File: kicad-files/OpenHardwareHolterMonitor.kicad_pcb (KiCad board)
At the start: 8 copper layers, 165 x 130 mm, 127 parts, among them CON1 Micro_SD_Card, J1 Conn_01x14, J10 Conn_01x01, J11 Conn_01x01, J12 USB_OTG, J13 USB_C_Receptacle, J2 Conn_01x01, J3 Conn_01x01, J4 Conn_01x01, J5 Conn_01x01, J6 Conn_01x01, J7 Conn_01x01, J8 Conn_01x01, J9 Conn_01x01, P1 Custom_FTDI, Q1 S8050, Q2 S8050, Q3 Q_NMOS_DGS, Q4 Q_NMOS_DGS, SW1 SW_SPDT, U1 ESP-WROOM-32, U2 ADS1298, U3 MCP73833, U4 MCP73833, U5 TPS2113A, U6 LP5912, U7 REM_3-xxxxS, Y1 32768Hz

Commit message: un-isolated power layout
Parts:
- added D11: LED, LEDs:LED_0603_HandSoldering, F.Cu at (206.4, 23.0)
- added D12: D_Schottky, Diodes_SMD:D_SOD-323_HandSoldering, F.Cu at (315.7, -50.1)
- added D13: D_Schottky, Diodes_SMD:D_SOD-323_HandSoldering, F.Cu at (325.9, -57.2)
- added D14: D_Schottky, Diodes_SMD:D_SOD-323_HandSoldering, F.Cu at (305.4, -43.1)
- added Q10: Q_PMOS_DGS, TO_SOT_Packages_SMD:SOT-23_Handsoldering, F.Cu at (306.4, -49.5)
- added Q5: Q_NMOS_DGS, TO_SOT_Packages_SMD:SOT-23W_Handsoldering, F.Cu at (296.1, -56.5)
- added Q6: Q_NMOS_DGS, TO_SOT_Packages_SMD:SOT-23W_Handsoldering, F.Cu at (296.1, -49.5)
- added Q7: Q_PMOS_DGS, TO_SOT_Packages_SMD:SOT-23_Handsoldering, F.Cu at (316.6, -56.5)
- added Q8: Q_PMOS_DGS, TO_SOT_Packages_SMD:SOT-23_Handsoldering, F.Cu at (306.4, -56.5)
- added Q9: Q_PMOS_DGS, TO_SOT_Packages_SMD:SOT-23_Handsoldering, F.Cu at (296.1, -42.4)
- added R37: 100k, Resistors_SMD:R_0603_HandSoldering, F.Cu at (322.3, -50.5)
- added R38: 100k, Resistors_SMD:R_0603_HandSoldering, F.Cu at (312.0, -43.5)
- added R39: 330, Resistors_SMD:R_0603_HandSoldering, F.Cu at (326.7, -41.7)
- added R40: 330, Resistors_SMD:R_0603_HandSoldering, F.Cu at (322.3, -45.5)
- added R41: 100k, Resistors_SMD:R_0603_HandSoldering, F.Cu at (326.7, -51.8)
- added R42: 100k, Resistors_SMD:R_0603_HandSoldering, F.Cu at (316.4, -44.7)
- added R43: 100k, Resistors_SMD:R_0603_HandSoldering, F.Cu at (320.8, -40.4)
- D7: value D_Schottky -> LED; footprint Diodes_SMD:D_SOD-323_HandSoldering -> LEDs:LED_0603_HandSoldering
- moved C40 159.0 mm to (202.2, -12.4)
- moved D3 159.0 mm to (222.2, -37.9)
- moved Q1 159.0 mm to (166.8, -42.8)
- moved Q4 159.0 mm to (198.2, -24.9)
- moved R12 159.0 mm to (178.8, -31.1)
- moved R27 159.0 mm to (213.4, -36.9)
- moved R28 159.0 mm to (203.8, -40.8)
- moved R29 159.0 mm to (195.6, -35.0)
- moved R30 159.0 mm to (208.8, -20.5)
- moved R31 159.0 mm to (165.8, -31.9)
- moved R32 159.0 mm to (215.6, -20.9)
- moved R34 159.0 mm to (202.1, -10.9)
- moved R7 159.0 mm to (188.2, -31.7)
- moved SW1 159.0 mm to (174.8, -37.9)
- moved TH1 159.0 mm to (192.4, -1.50)
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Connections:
- BT1 pad 1: /Vbat2 -> Net-(BT1-Pad1)
- BT2 pad 1: /Vbat1 -> Net-(BT2-Pad1)
- D6 pad 2: /Vbat2 -> Net-(D6-Pad2)
- D7 pad 1: /power/REGULATOR_IN -> /power/Bat1_backwards
- D7 pad 2: /Vbat1 -> GND
- J1 pad 10: /IO27 -> /IO36
- J1 pad 11: /IO36 -> /IO39
- J1 pad 12: /IO39 -> /Enable_Charging
- J1 pad 9: /IO26 -> /IO27
- R29 pad 2: GND -> Net-(Q6-Pad1)
- R30 pad 2: GND -> Net-(Q5-Pad1)
- R36 pad 1: GND -> Net-(D9-Pad1)
- R36 pad 2: Net-(D9-Pad1) -> GND
- U1 pad 11: /IO26 -> /Enable_Charging
- U3 pad 10: /Vbat2 -> Net-(D6-Pad2)
- U3 pad 9: /Vbat2 -> Net-(D6-Pad2)
- U4 pad 10: /Vbat1 -> Net-(D12-Pad2)
- U4 pad 9: /Vbat1 -> Net-(D12-Pad2)

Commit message: board layout checkpoint
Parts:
- added TP5: Test_Point, Measurement_Points:Measurement_Point_Square-SMD-Pad_Small, F.Cu at (244.5, -66.0)
- added TP6: Test_Point, Measurement_Points:Measurement_Point_Square-SMD-Pad_Small, F.Cu at (236.3, -60.0)
- added TP7: Test_Point, Measurement_Points:Measurement_Point_Square-SMD-Pad_Small, F.Cu at (236.3, -66.0)
- J1: value Conn_01x14 -> Conn_02x06_Odd_Even; footprint Pin_Headers:Pin_Header_Straight_1x14_Pitch2.54mm -> Pin_Headers:Pin_Header_Straight_2x06_Pitch1.27mm
- TP1, TP2, TP3, TP4: value TEST -> Test_Point; footprint Measurement_Points:Measurement_Point_Round-SMD-Pad_Small -> Measurement_Points:Measurement_Point_Square-SMD-Pad_Small
- moved P1 33.5 mm to (171.5, 23.0), turned to 180 degrees
- moved CON1 33.0 mm to (182.5, 27.5)
- moved C38 28.3 mm to (172.0, 85.0)
- moved J1 23.3 mm to (150.0, 42.5)
- moved C34 22.0 mm to (146.0, 72.2)
- moved C35 22.0 mm to (146.0, 63.0)
- moved C37 22.0 mm to (146.0, 82.0)
- moved U1 15.0 mm to (156.0, 30.5), turned to 90 degrees
- moved U5 14.1 mm to (158.5, 83.5)
- moved FL1 13.5 mm to (167.0, 76.5)
- moved R35 13.5 mm to (155.0, 76.5)
- moved U7 13.4 mm to (164.0, 58.0)
- moved D8 13.0 mm to (166.0, 64.4)
- moved C39 12.7 mm to (159.5, 66.0)
- moved C41 12.7 mm to (159.0, 61.0)
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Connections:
- J1 pad 10: /IO36 -> /IO27
- J1 pad 11: /IO39 -> /IO36
- J1 pad 12: /Enable_Charging -> /IO39
- J1 pad 2: +3V3 -> GND
- J1 pad 3: /IO2 -> +3V3
- J1 pad 4: /IO4 -> /IO2
- J1 pad 5: /IO12 -> /IO4
- J1 pad 6: /IO13 -> /IO12
- J1 pad 7: /IO14 -> /IO13
- J1 pad 8: /IO15 -> /IO14
- J1 pad 9: /IO27 -> /IO15
- TP1 pad 1: Net-(TP1-Pad1) -> /Enable_Charging
- TP2 pad 1: Net-(TP2-Pad1) -> /Vbat1
- TP3 pad 1: Net-(TP3-Pad1) -> /Vbat2
- U3 pad 4: Net-(TP1-Pad1) -> Net-(TP5-Pad1)
- U3 pad 7: Net-(TP3-Pad1) -> Net-(TP7-Pad1)
- U4 pad 4: Net-(TP2-Pad1) -> Net-(TP4-Pad1)
- U4 pad 7: Net-(TP4-Pad1) -> Net-(TP6-Pad1)

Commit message: checkpoint PCB
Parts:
- moved R35 3.16 mm to (156.0, 73.5), turned to 0 degrees
- moved U5 2.92 mm to (157.0, 81.0), turned to 270 degrees
- moved P1 1.12 mm to (171.0, 22.0)
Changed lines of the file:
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@@
   (general
     (thickness 1.6)
-    (drawings 17)
+    (drawings 16)
     (tracks 336)
     (zones 0)
@@
   )
   (module Pin_Headers:Pin_Header_Straight_1x07_Pitch2.54mm (layer B.Cu)
-    (at 171.5 23 180)
+    (at 171 22 180)
     (descr "Through hole straight pin header, 1x07, 2.54mm pitch, single row")
     (tags "Through hole pin header THT 1x07 2.54mm single row")
@@
   )
   (module Resistors_SMD:R_0603_HandSoldering (layer F.Cu)
-    (at 155 76.5 270)
+    (at 156 73.5)
     (descr "Resistor SMD 0603, hand soldering")
     (tags "resistor 0603")
     (attr smd)
-    (fp_text reference R35 (at 0 -1.45 270) (layer F.SilkS)
+    (fp_text reference R35 (at 0 -1.45) (layer F.SilkS)
       (effects (font (size 1 1) (thickness 0.15)))
     )
-    (fp_text value 1k (at 0 1.55 270) (layer F.Fab)
+    (fp_text value 1k (at 0 1.55) (layer F.Fab)
       (effects (font (size 1 1) (thickness 0.15)))
     )
-    (fp_text user %R (at -0.6 0.75 270) (layer F.Fab)
+    (fp_text user %R (at -0.6 0.75) (layer F.Fab)
       (effects (font (size 0.4 0.4) (thickness 0.075)))
     )
@@
     (fp_line (start 1.95 0.7) (end 1.95 -0.7) (layer F.CrtYd) (width 0.05))
     (fp_line (start 1.95 0.7) (end -1.96 0.7) (layer F.CrtYd) (width 0.05))
-    (pad 1 smd rect (at -1.1 0 270) (size 1.2 0.9) (layers F.Cu F.Paste F.Mask)
+    (pad 1 smd rect (at -1.1 0) (size 1.2 0.9) (layers F.Cu F.Paste F.Mask)
       (net 108 "Net-(R35-Pad1)"))
-    (pad 2 smd rect (at 1.1 0 270) (size 1.2 0.9) (layers F.Cu F.Paste F.Mask)
+    (pad 2 smd rect (at 1.1 0) (size 1.2 0.9) (layers F.Cu F.Paste F.Mask)
       (net 25 GNDPWR))
     (model ${KISYS3DMOD}/Resistors_SMD.3dshapes/R_0603.wrl
@@
   )
   (module Housings_SSOP:TSSOP-8_4.4x3mm_Pitch0.65mm (layer F.Cu)
-    (at 158.5 83.5 180)
+    (at 157 81 270)
     (descr "8-Lead Plastic Thin Shrink Small Outline (ST)-4.4 mm Body [TSSOP] (see Microchip Packaging Specification 00000049BS.pdf)")
     (tags "SSOP 0.65")
     (attr smd)
-    (fp_text reference U5 (at 0 -2.55 180) (layer F.SilkS)
+    (fp_text reference U5 (at 0 -2.55 270) (layer F.SilkS)
       (effects (font (size 1 1) (thickness 0.15)))
     )
-    (fp_text value TPS2113A (at 0 2.55 180) (layer F.Fab)
+    (fp_text value TPS2113A (at 0 2.55 270) (layer F.Fab)
       (effects (font (size 1 1) (thickness 0.15)))
     )
-    (fp_text user %R (at 0 0 180) (layer F.Fab)
+    (fp_text user %R (at 0 0 270) (layer F.Fab)
       (effects (font (size 0.7 0.7) (thickness 0.15)))
     )
@@
     (fp_line (start 2.2 -1.5) (end 2.2 1.5) (layer F.Fab) (width 0.15))
     (fp_line (start -1.2 -1.5) (end 2.2 -1.5) (layer F.Fab) (width 0.15))
-    (pad 8 smd rect (at 2.95 -0.975 180) (size 1.45 0.45) (layers F.Cu F.Paste F.Mask)
+    (pad 8 smd rect (at 2.95 -0.975 270) (size 1.45 0.45) (layers F.Cu F.Paste F.Mask)
       (net 27 /power/USB_MICRO_IN))
-    (pad 7 smd rect (at 2.95 -0.325 180) (size 1.45 0.45) (layers F.Cu F.Paste F.Mask)
+    (pad 7 smd rect (at 2.95 -0.325 270) (size 1.45 0.45) (layers F.Cu F.Paste F.Mask)
       (net 24 /power/MUX_POWER_OUT))
-    (pad 6 smd rect (at 2.95 0.325 180) (size 1.45 0.45) (layers F.Cu F.Paste F.Mask)
+    (pad 6 smd rect (at 2.95 0.325 270) (size 1.45 0.45) (layers F.Cu F.Paste F.Mask)
       (net 26 /power/USB_C_IN))
-    (pad 5 smd rect (at 2.95 0.975 180) (size 1.45 0.45) (layers F.Cu F.Paste F.Mask)
+    (pad 5 smd rect (at 2.95 0.975 270) (size 1.45 0.45) (layers F.Cu F.Paste F.Mask)
       (net 25 GNDPWR))
-    (pad 4 smd rect (at -2.95 0.975 180) (size 1.45 0.45) (layers F.Cu F.Paste F.Mask)
+    (pad 4 smd rect (at -2.95 0.975 270) (size 1.45 0.45) (layers F.Cu F.Paste F.Mask)
       (net 108 "Net-(R35-Pad1)"))
-    (pad 3 smd rect (at -2.95 0.325 180) (size 1.45 0.45) (layers F.Cu F.Paste F.Mask)
+    (pad 3 smd rect (at -2.95 0.325 270) (size 1.45 0.45) (layers F.Cu F.Paste F.Mask)
       (net 25 GNDPWR))
-    (pad 2 smd rect (at -2.95 -0.325 180) (size 1.45 0.45) (layers F.Cu F.Paste F.Mask)
+    (pad 2 smd rect (at -2.95 -0.325 270) (size 1.45 0.45) (layers F.Cu F.Paste F.Mask)
       (net 25 GNDPWR))
-    (pad 1 smd rect (at -2.95 -0.975 180) (size 1.45 0.45) (layers F.Cu F.Paste F.Mask)
+    (pad 1 smd rect (at -2.95 -0.975 270) (size 1.45 0.45) (layers F.Cu F.Paste F.Mask)
       (net 116 "Net-(U5-Pad1)"))
     (model ${KISYS3DMOD}/Housings_SSOP.3dshapes/TSSOP-8_4.4x3mm_Pitch0.65mm.wrl
@@
   (gr_line (start 124.5 105) (end 125 105) (layer F.SilkS) (width 0.2))
   (gr_line (start 105 67.5) (end 105 150) (layer Edge.Cuts) (width 0.15))
-  (gr_line (start 194 -46.5) (end 194 -86) (layer F.SilkS) (width 0.2))
   (gr_line (start 270 20) (end 125 20) (layer Edge.Cuts) (width 0.15))
   (gr_line (start 270 100) (end 125 100) (layer Edge.Cuts) (width 0.15))

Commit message: charger layout
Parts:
- moved D13 192.5 mm to (212.0, 98.0)
- moved R40 188.9 mm to (196.0, 95.0)
- moved R41 185.5 mm to (211.4, 93.5)
- moved R42 185.4 mm to (192.0, 92.8)
- moved Q8 181.8 mm to (197.1, 88.7)
- moved R43 181.7 mm to (184.0, 79.2)
- moved Q10 181.3 mm to (189.0, 88.8), turned to 180 degrees
- moved R38 180.2 mm to (184.0, 83.2)
- moved Q7 175.1 mm to (220.0, 89.5)
- moved R39 174.0 mm to (219.0, 95.0)
- moved R37 169.8 mm to (220.0, 85.0)
- moved D14 161.8 mm to (190.0, 70.2)
- moved Q6 161.4 mm to (192.5, 74.2)
- moved D12 161.0 mm to (223.0, 81.5), turned to 270 degrees
- moved Q9 156.2 mm to (212.5, 89.5), turned to 180 degrees
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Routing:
- net Net-(C33-Pad1): track 52.9 -> 53.5 mm

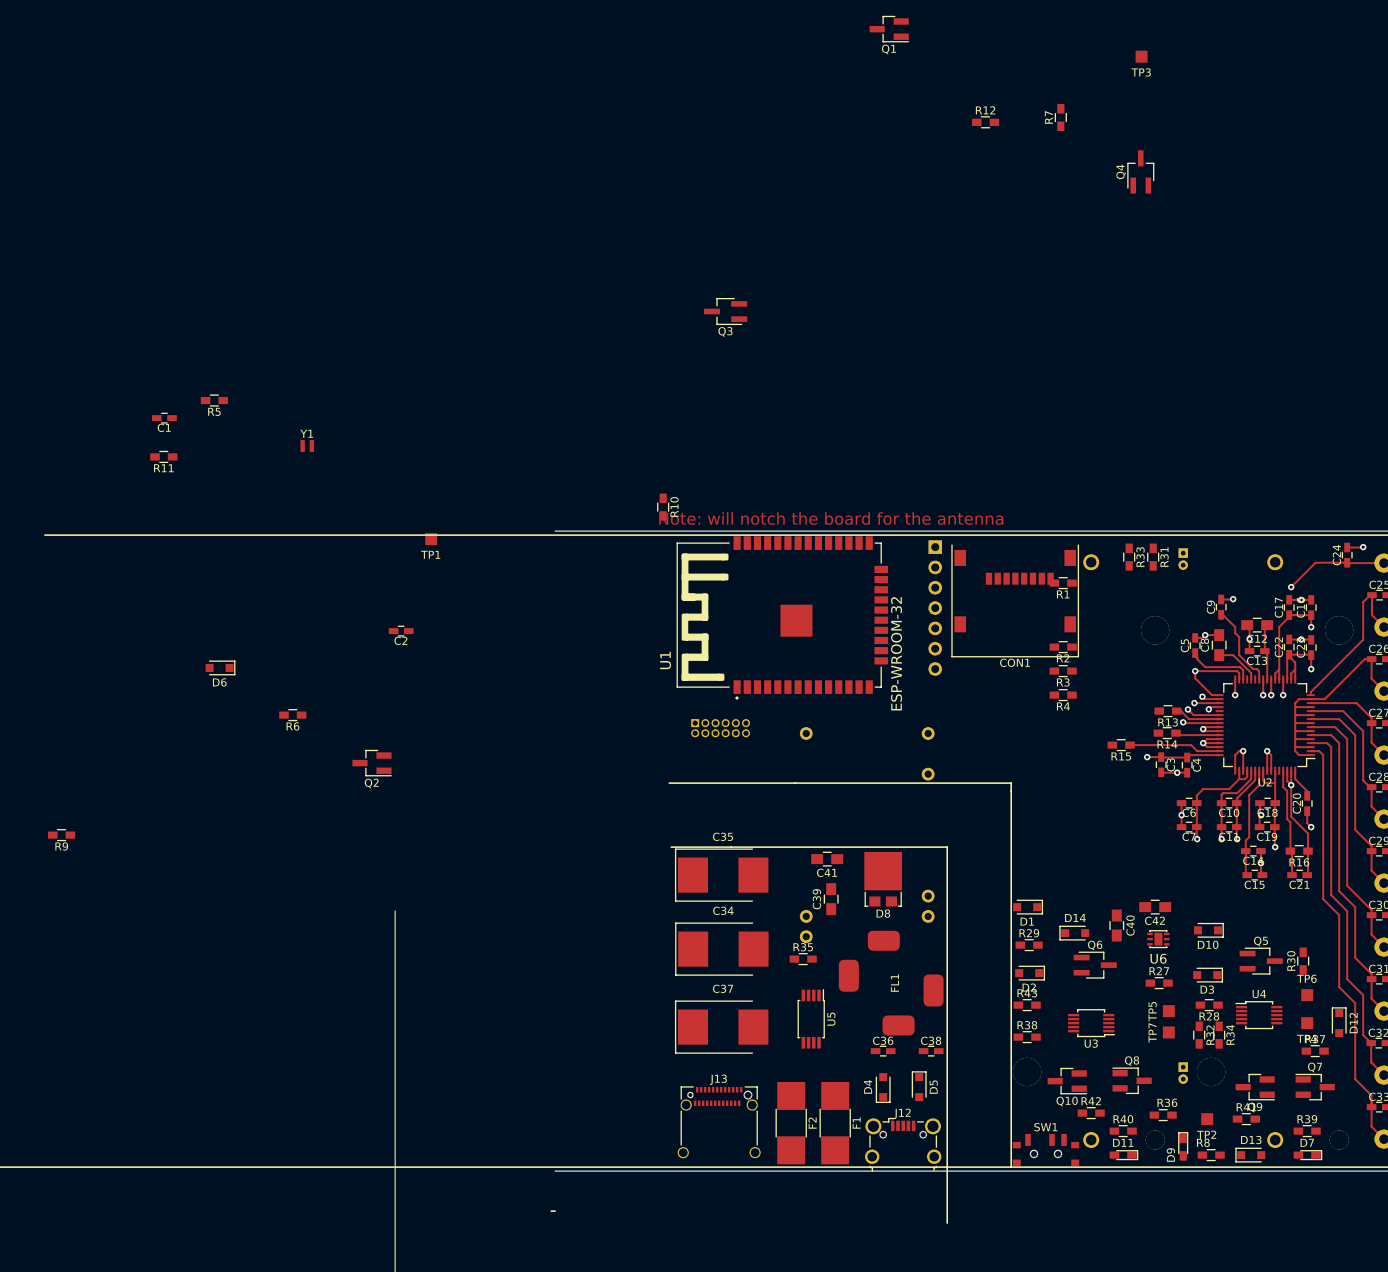
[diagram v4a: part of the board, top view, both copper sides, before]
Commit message: initial hook-up of isolated side
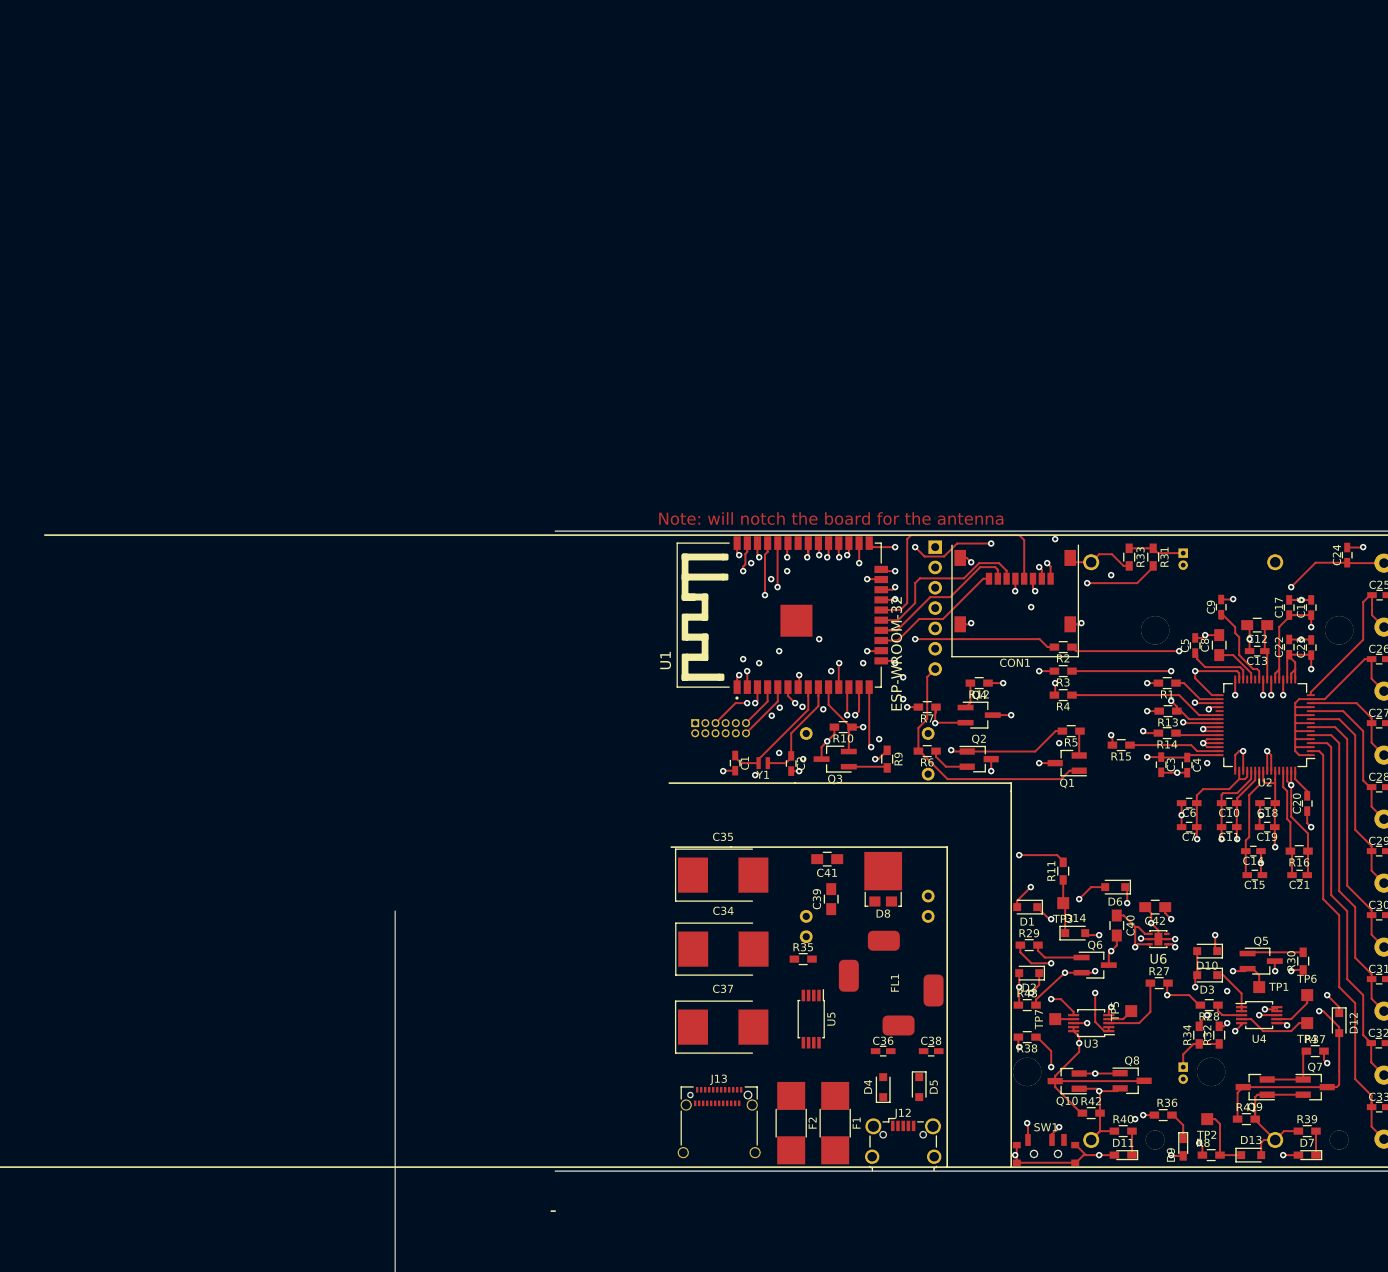
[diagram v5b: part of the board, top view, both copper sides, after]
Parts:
- moved R11 123.8 mm to (188.5, 62.5), turned to 90 degrees
- moved TP1 117.7 mm to (213.0, 77.0), turned to 0 degrees
- moved D6 115.3 mm to (195.0, 64.5)
- moved R5 114.8 mm to (189.5, 45.0)
- moved TP3 106.3 mm to (188.5, 66.5)
- moved R9 103.6 mm to (166.5, 48.5), turned to 270 degrees
- moved Q1 94.4 mm to (189.0, 49.0)
- moved C1 83.4 mm to (147.5, 49.0), turned to 270 degrees
- moved R6 79.4 mm to (171.5, 47.5)
- moved Q2 75.9 mm to (178.0, 48.5), turned to 0 degrees
- moved R7 75.6 mm to (171.5, 42.0), turned to 180 degrees
- moved Q4 70.8 mm to (178.0, 43.0), turned to 0 degrees
- moved R12 70.1 mm to (178.0, 39.0), turned to 180 degrees
- moved Y1 69.4 mm to (151.0, 49.0), turned to 0 degrees
- moved Q3 57.6 mm to (160.0, 48.5)
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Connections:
- SW1 pad GND: (no net) -> GND
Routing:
- net /read_bat_1: track 0.00 -> 112.9 mm, vias 0 -> 5
- net /Enable_Charging: track 0.00 -> 100.6 mm, vias 0 -> 7
- net /power/REGULATOR_IN: track 0.00 -> 81.2 mm, vias 0 -> 6
- net /~RESET~_OUT: track 1.46 -> 75.4 mm, vias 1 -> 3
- net /power/V_ISO: track 0.00 -> 73.6 mm, vias 0 -> 2
- net /~PWDN~_OUT: track 3.15 -> 76.7 mm, vias 1 -> 5
- net GND: track 100.7 -> 173.2 mm, vias 30 -> 56
- net /MOSI: track 0.00 -> 68.5 mm, vias 0 -> 3
- net Net-(R31-Pad2): track 0.00 -> 65.9 mm, vias 0 -> 2
- net /MISO: track 0.00 -> 65.9 mm, vias 0 -> 3
- net /read_bat_2: track 0.00 -> 57.7 mm, vias 0 -> 3
- net /~DRDY~_IN: track 0.00 -> 56.9 mm, vias 0 -> 3
- net /FTDI_V: track 0.00 -> 50.3 mm, vias 0 -> 2
- net /START_OUT: track 0.00 -> 49.8 mm, vias 0 -> 3
- net /EN: track 0.00 -> 49.2 mm, vias 0 -> 3
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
